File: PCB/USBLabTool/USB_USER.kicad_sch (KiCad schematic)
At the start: 17 parts, among them J20 USB_C_Receptacle, Q1 STL11N3LLH6, U17 TCPP01-M12

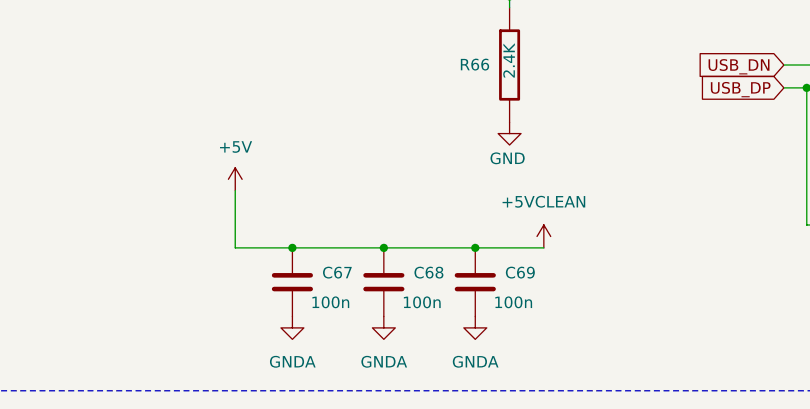
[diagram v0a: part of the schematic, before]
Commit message: fixed grounds for several components and fix 5V clean
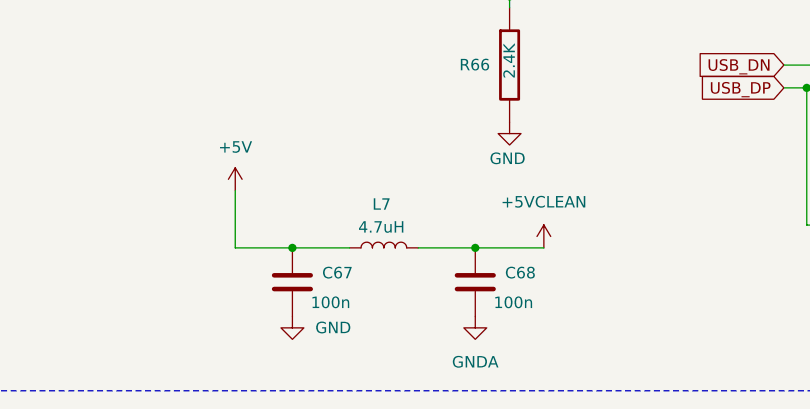
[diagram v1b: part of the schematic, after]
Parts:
- removed C69: 100n, Capacitor_SMD:C_0603_1608Metric_Pad1.08x0.95mm_HandSolder, symbol Device:C
- added L7: 4.7uH, Inductor_SMD:L_0603_1608Metric_Pad1.05x0.95mm_HandSolder, symbol Device:L
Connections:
- net +5V: now also L7.1; no longer C68.1
- net GND: now also C67.2
- net GNDA: no longer C67.2
- new net +5VCLEAN: C68.1, L7.2
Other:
- moved on the sheet: C68

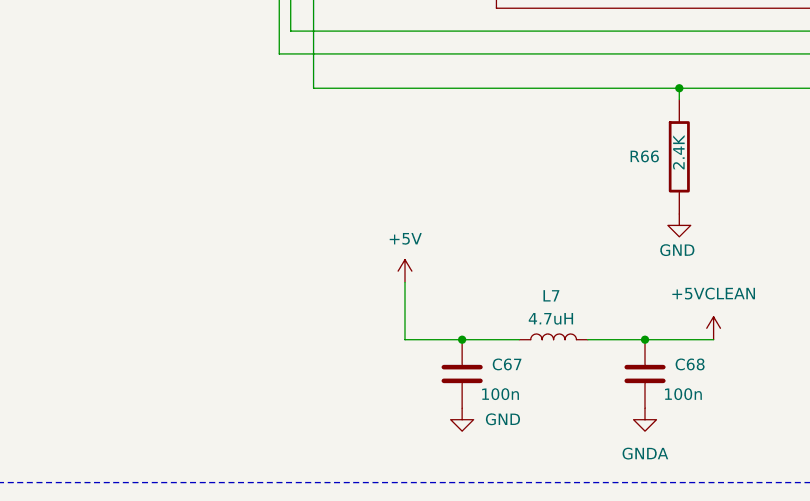
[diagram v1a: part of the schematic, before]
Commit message: PCB updates from meeting 3/19
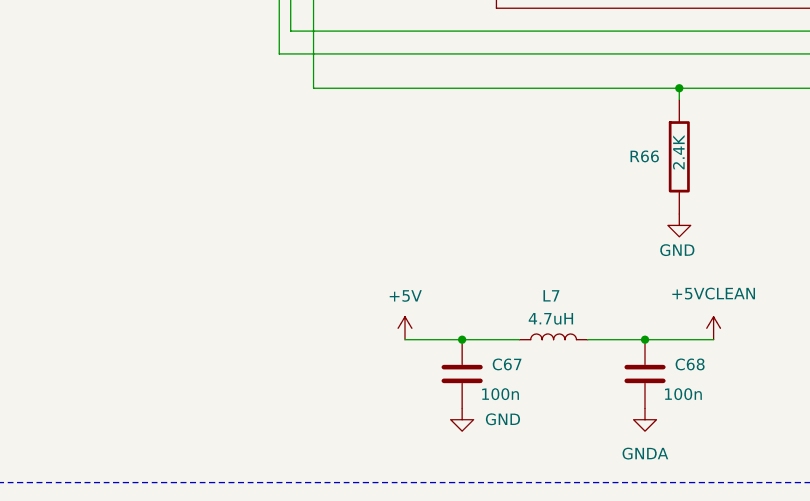
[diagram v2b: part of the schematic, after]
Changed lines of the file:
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@@
-	(wire
-		(pts
-			(xy 121.92 140.97) (xy 121.92 147.32)
-		)
-		(stroke
-			(width 0)
-			(type default)
-		)
-	)
 	(wire
 		(pts
@@
 	(symbol
 		(lib_id "power:+5V")
-		(at 121.92 140.97 0)
+		(at 121.92 147.32 0)
 		(unit 1)
 		(exclude_from_sim no)
@@
 		(fields_autoplaced yes)
 		(property "Reference" "#PWR0130"
-			(at 121.92 144.78 0)
+			(at 121.92 151.13 0)
 			(effects
 				(font
@@
 		)
 		(property "Value" "+5V"
-			(at 121.92 136.144 0)
+			(at 121.92 142.494 0)
 			(effects
 				(font
@@
 		)
 		(property "Footprint" ""
-			(at 121.92 140.97 0)
+			(at 121.92 147.32 0)
 			(effects
 				(font
@@
 		)
 		(property "Datasheet" ""
-			(at 121.92 140.97 0)
+			(at 121.92 147.32 0)
 			(effects
 				(font
@@
 		)
 		(property "Description" ""
-			(at 121.92 140.97 0)
-			(effects
-				(font
+			(at 121.92 147.32 0)
+			(effects
+				(font

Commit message: change USB footprint, fix some warnings and problems
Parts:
- J20: footprint Connector_USB:USB_C_Receptacle_Amphenol_12401548E4-2A -> userfp:AMPHENOL_12401832E402A
- U17: footprint QFN12_TCPP01-M12_STM -> userfp:QFN12_TCPP01-M12_STM
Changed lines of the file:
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@@
 			)
 		)
-		(property "Footprint" "Connector_USB:USB_C_Receptacle_Amphenol_12401548E4-2A"
+		(property "Footprint" "userfp:AMPHENOL_12401832E402A"
 			(at 238.76 95.25 0)
 			(effects
@@
 			)
 		)
-		(property "Footprint" "QFN12_TCPP01-M12_STM"
+		(property "Footprint" "userfp:QFN12_TCPP01-M12_STM"
 			(at 124.46 90.17 0)
 			(effects

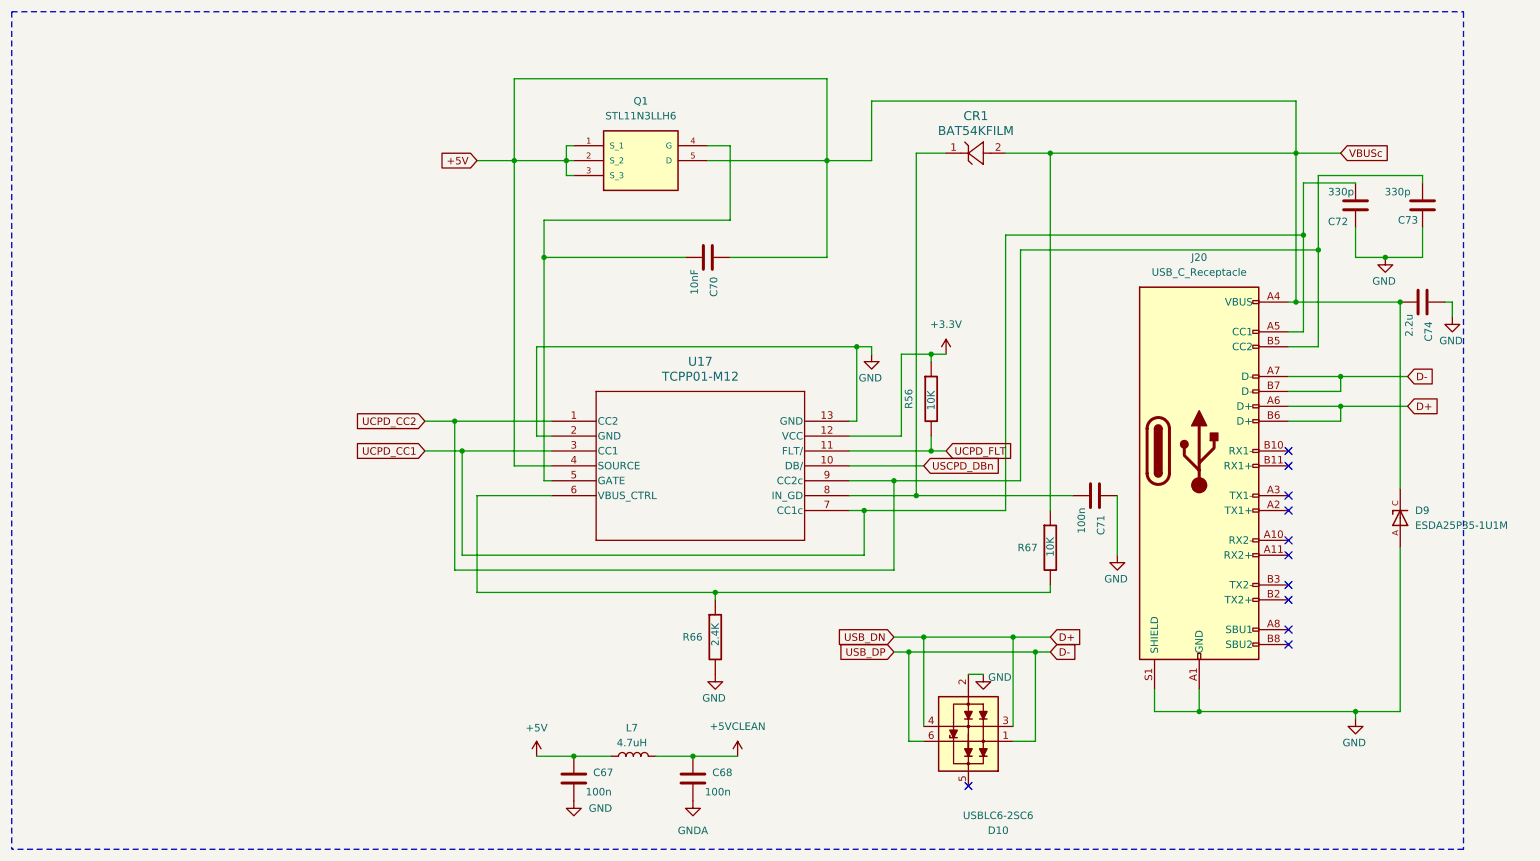
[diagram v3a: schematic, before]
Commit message: Resolved DRC/ERC errors in PCB and schematic
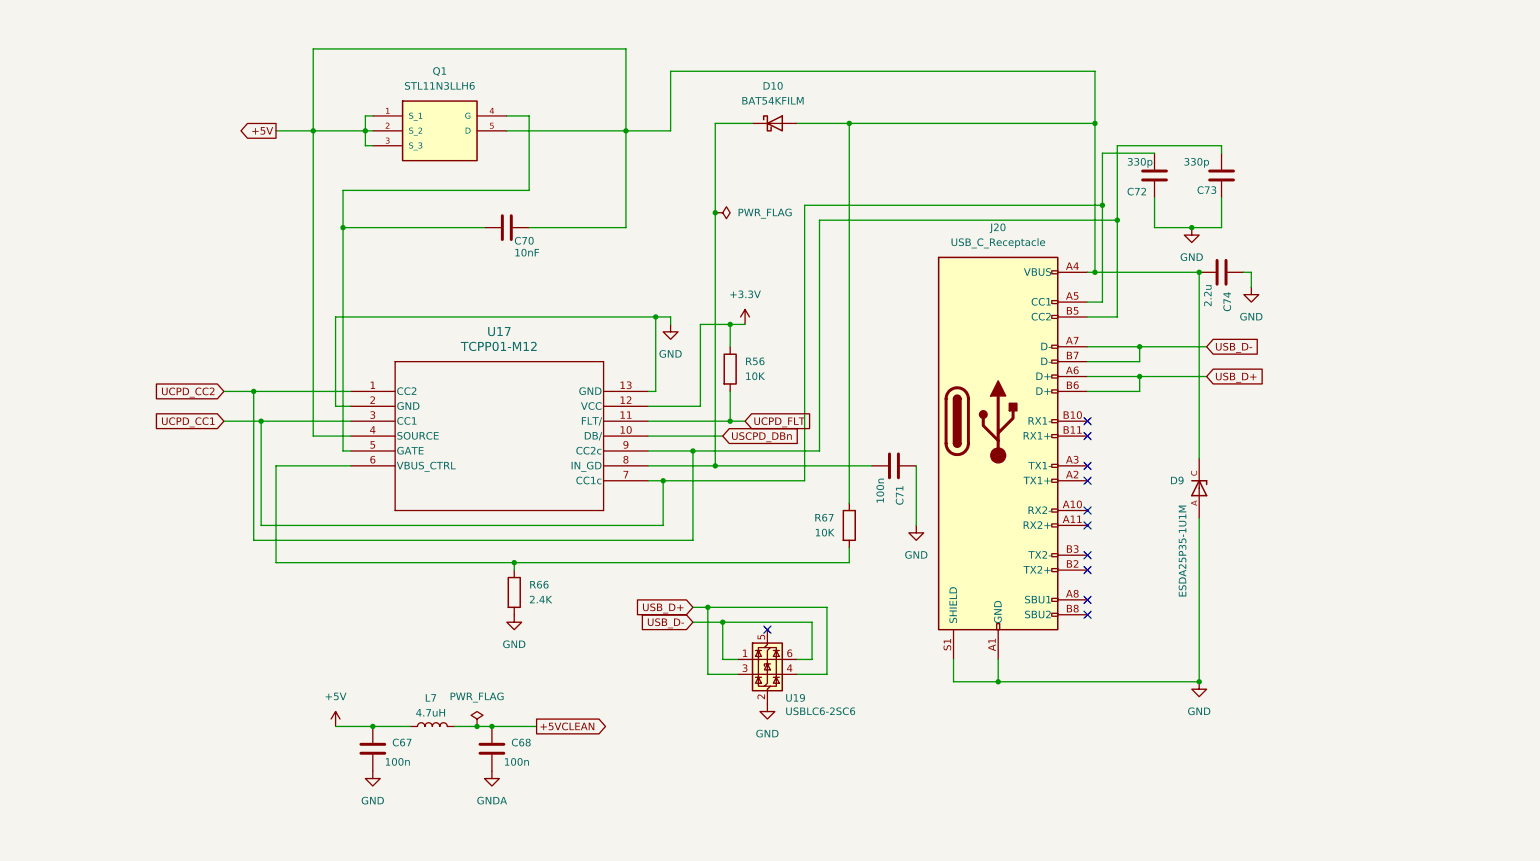
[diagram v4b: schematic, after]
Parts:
- removed CR1: BAT54KFILM, Diode_SMD:D_SOD-523, symbol BAT54KFILM:BAT54KFILM
- removed D10: USBLC6-2SC6, userfp:SOT95P280X145-6N, symbol PCM_Diode_TVS_AKL:USBLC6-2SC6
- removed D9: ESDA25P35-1U1M, userfp:TVS_ESDA25P35-1U1M, symbol ESDA25P35-1U1M:ESDA25P35-1U1M
- removed Q1: STL11N3LLH6, userfp:STL20N6F7_snapmagic, symbol STL11N3LLH6_snapmagic:STL11N3LLH6
- removed R56, R67: 10K, Resistor_SMD:R_0603_1608Metric, symbol freetronics_schematic:R
- removed R66: 2.4K, Resistor_SMD:R_0603_1608Metric, symbol freetronics_schematic:R
- removed U17: TCPP01-M12, userfp:QFN12_TCPP01-M12_STM, symbol TCPP01-M12:TCPP01-M12
- added D10: BAT54KFILM, Diode_SMD:D_SOD-523, symbol Device:D_Schottky
- added D9: ESDA25P35-1U1M, userfp:TVS_ESDA25P35-1U1M, symbol USBLabTool:ESDA25P35-1U1M
- added Q1: STL11N3LLH6, userfp:STL20N6F7, symbol USBLabTool:STL11N3LLH6
- added R56, R67: 10K, Resistor_SMD:R_0603_1608Metric, symbol Device:R
- added R66: 2.4K, Resistor_SMD:R_0603_1608Metric, symbol Device:R
- added U17: TCPP01-M12, userfp:QFN12_TCPP01-M12_STM, symbol USBLabTool:TCPP01-M12
- added U19: USBLC6-2SC6, Package_TO_SOT_SMD:SOT-23-6, symbol Power_Protection:USBLC6-2SC6
- J20: footprint userfp:AMPHENOL_12401832E402A -> Connector_USB:USB_C_Receptacle_Amphenol_12401610E4-2A
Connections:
- net +3.3V: now also R56.1, U17.12 (VCC)
- net +5V: now also D10.2 (A), D9.C, Q1.1 (S_1), Q1.2 (S_2), Q1.3 (S_3), Q1.5 (D), R67.1, U17.4 (SOURCE)
- net GND: now also D9.A, R66.2, U17.13 (GND), U17.2 (GND), U19.2 (GND)
- net UCPD_CC1: now also U17.3 (CC1), U17.7 (CC1c)
- net UCPD_CC2: now also U17.1 (CC2), U17.9 (CC2c)
- net UCPD_FLT: now also R56.2, U17.11 (FLT/)
- net USCPD_DBn: now also U17.10 (DB/)
- net at C70.2: now also Q1.4 (G), U17.5 (GATE)
- net at C71.2: now also D10.1 (K), U17.8 (IN_GD)
- net D+ renamed USB_D+
- net USB_D+: now also U19.3 (I/O2), U19.4 (I/O2)
- net D- renamed USB_D-
- net USB_D-: now also U19.1 (I/O1), U19.6 (I/O1)
- new net: R66.1, R67.2, U17.6 (VBUS_CTRL)
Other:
- moved on the sheet: C67, C68, C70, C71, C72, C73, C74, J20, L7
